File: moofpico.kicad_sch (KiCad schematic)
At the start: 21 parts, among them J1 Conn_01x04, J100 Bus_Apple_II_Card_Side, J2 Micro_SD_Card_Det2, Q1 BS170, SW1 SW_DIP_x02, U2 74F11, U3 74LVC245, U4 74LVC245, U5 74LVC245, U6 RaspberryPi_Pico

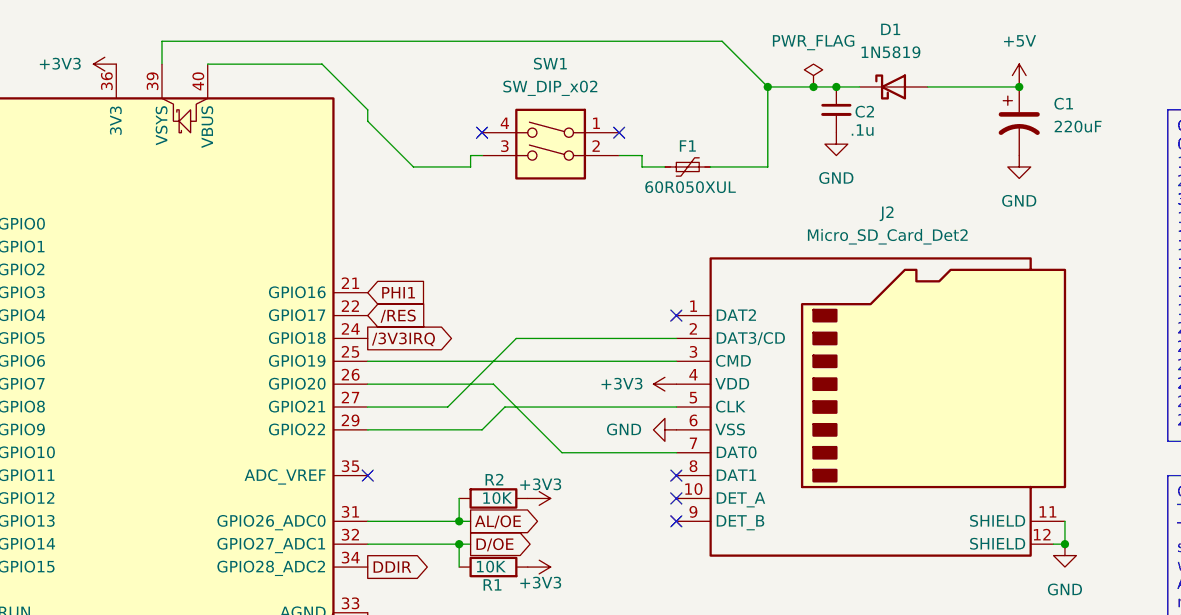
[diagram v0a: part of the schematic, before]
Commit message: checkpoint: kicad 8.0.1, move components around
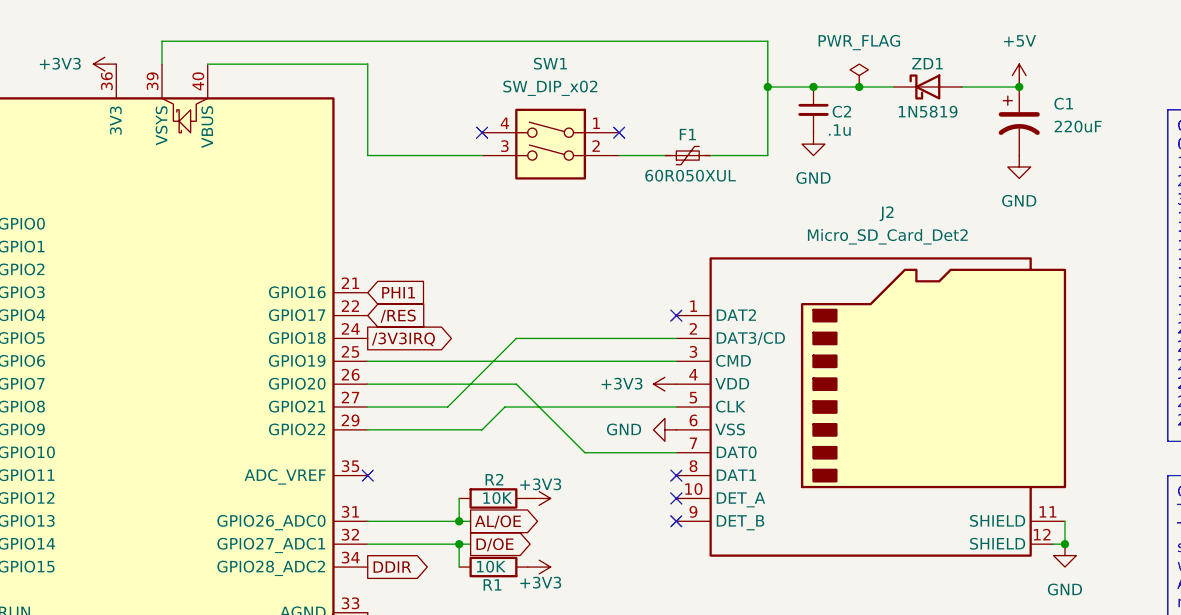
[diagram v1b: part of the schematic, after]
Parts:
- renumbered D1 to ZD1
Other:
- moved on the sheet: C2, F1, ZD1

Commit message: probably voodoo at this point, but: add another decoupling cap (although I seriously doubt it's needed at this point) provide enough space on the board so q1, c1, and f1 can all be bent flat
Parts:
- added C6: .1u, Capacitor_THT:C_Disc_D3.8mm_W2.6mm_P2.50mm, symbol Device:C_Small
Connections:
- net +3V3: now also C6.1
- net GND: now also C6.2
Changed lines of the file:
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@@
 	)
 	(junction
+		(at 41.91 142.24)
+		(diameter 0)
+		(color 0 0 0 0)
+	)
+	(junction
 		(at 57.15 91.44)
 		(diameter 0)
@@
 	(wire
 		(pts
+			(xy 41.91 142.24) (xy 50.8 142.24)
+		)
+		(stroke
+			(width 0)
+			(type default)
+		)
+	)
+	(wire
+		(pts
+			(xy 33.02 137.16) (xy 41.91 137.16)
+		)
+		(stroke
+			(width 0)
+			(type default)
+		)
+	)
+	(wire
+		(pts
 			(xy 118.11 152.4) (xy 119.38 152.4)
 		)
@@
 	(wire
 		(pts
+			(xy 33.02 142.24) (xy 41.91 142.24)
+		)
+		(stroke
+			(width 0)
+			(type default)
+		)
+	)
+	(wire
+		(pts
 			(xy 144.78 177.8) (xy 148.59 177.8)
 		)
@@
 	)
 	(symbol
-		(lib_id "power:GND")
-		(at 50.8 142.24 0)
-		(unit 1)
-		(exclude_from_sim no)
-		(in_bom yes)
-		(on_board yes)
-		(dnp no)
-		(fields_autoplaced yes)
-		(property "Reference" "#PWR038"
-			(at 50.8 148.59 0)
-			(effects
-				(font
-					(size 1.27 1.27)
-				)
-				(hide yes)
-			)
-		)
-		(property "Value" "GND"
-			(at 50.8 147.32 0)
-			(effects
-				(font
-					(size 1.27 1.27)
-				)
-			)
-		)
-		(property "Footprint" ""
-			(at 50.8 142.24 0)
-			(effects
-				(font
-					(size 1.27 1.27)
-				)
-				(hide yes)
-			)
-		)
-		(property "Datasheet" ""
-			(at 50.8 142.24 0)
-			(effects
-				(font
-					(size 1.27 1.27)
-				)
-				(hide yes)
-			)
-		)
-		(property "Description" "Power symbol creates a global label with name \"GND\" , ground"
-			(at 50.8 142.24 0)
-			(effects
-				(font
-					(size 1.27 1.27)
-				)
-				(hide yes)
-			)
-		)
-		(pin "1"
-		)
-		(instances
-			(project "moofpico"
-				(path "/adf04048-7c47-4d7c-943c-c55ccf696419"
-					(reference "#PWR038")
-					(unit 1)
-				)
-			)
-		)
-	)
-	(symbol
 		(lib_id "Transistor_FET:BS170")
 		(at 99.06 172.72 0)
@@
 					(unit 1)
 				)
+			)
+		)
+	)
+	(symbol
+		(lib_id "Device:C_Small")
+		(at 33.02 139.7 0)
+		(unit 1)
+		(exclude_from_sim no)
+		(in_bom yes)
+		(on_board yes)
+		(dnp no)
+		(fields_autoplaced yes)
+		(property "Reference" "C6"
+			(at 35.56 138.4362 0)
+			(effects
+				(font
+					(size 1.27 1.27)
+				)
+				(justify left)
+			)
+		)
+		(property "Value" ".1u"
+			(at 35.56 140.9762 0)
+			(effects
+				(font
+					(size 1.27 1.27)
+				)
+				(justify left)
+			)
+		)
+		(property "Footprint" "Capacitor_THT:C_Disc_D3.8mm_W2.6mm_P2.50mm"
+			(at 33.02 139.7 0)
+			(effects
+				(font
+					(size 1.27 1.27)
+				)
+				(hide yes)
+			)
+		)
+		(property "Datasheet" "https://www.vishay.com/docs/45171/kseries.pdf"
+			(at 33.02 139.7 0)
+			(effects
+				(font
+					(size 1.27 1.27)
+				)
+				(hide yes)
+			)
+		)
+		(property "Description" "K104K10X7RF53L2"
+			(at 33.02 139.7 0)
+			(effects
+				(font
+					(size 1.27 1.27)
+				)
+				(hide yes)
+			)
+		)
+		(pin "1"
+		)
+		(pin "2"
+		)
+		(instances
+			(project "moofpico"
+				(path "/adf04048-7c47-4d7c-943c-c55ccf696419"
+					(reference "C6")
+					(unit 1)
+				)

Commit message: swap nand pin assignments around
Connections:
- net TTLENBL: now also U2.12; no longer U2.8
- net at J100.1 (~{I/O_SELECT}): now also U2.2; no longer U2.9
- net at J100.20 (~{I/O_STROBE}): now also U2.13; no longer U2.11
- net at J100.41 (~{DEVICE_SELECT}): now also U2.1; no longer U2.10
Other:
- moved on the sheet: U2A, U2C
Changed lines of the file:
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@@
 	(wire
 		(pts
-			(xy 161.29 142.24) (xy 176.53 142.24)
-		)
-		(stroke
-			(width 0)
-			(type default)
-		)
-	)
-	(wire
-		(pts
 			(xy 144.78 124.46) (xy 156.21 124.46)
 		)
@@
 	(wire
 		(pts
-			(xy 147.32 142.24) (xy 144.78 142.24)
-		)
-		(stroke
-			(width 0)
-			(type default)
-		)
-	)
-	(wire
-		(pts
 			(xy 199.39 21.59) (xy 203.2 21.59)
 		)
@@
 	(wire
 		(pts
-			(xy 144.78 139.7) (xy 176.53 139.7)
-		)
-		(stroke
-			(width 0)
-			(type default)
-		)
-	)
-	(wire
-		(pts
 			(xy 144.78 29.21) (xy 157.48 29.21)
 		)
@@
 	(wire
 		(pts
-			(xy 144.78 137.16) (xy 156.21 137.16)
-		)
-		(stroke
-			(width 0)
-			(type default)
-		)
-	)
-	(wire
-		(pts
 			(xy 168.91 62.23) (xy 179.07 62.23)
 		)
@@
 	(wire
 		(pts
-			(xy 147.32 144.78) (xy 147.32 142.24)
-		)
-		(stroke
-			(width 0)
-			(type default)
-		)
-	)
-	(wire
-		(pts
 			(xy 144.78 52.07) (xy 179.07 52.07)
 		)
@@
 	(wire
 		(pts
-			(xy 147.32 144.78) (xy 176.53 144.78)
-		)
-		(stroke
-			(width 0)
-			(type default)
-		)
-	)
-	(wire
-		(pts
 			(xy 144.78 69.85) (xy 154.94 69.85)
 		)
@@
 	(wire
 		(pts
-			(xy 156.21 137.16) (xy 161.29 142.24)
-		)
-		(stroke
-			(width 0)
-			(type default)
-		)
-	)
-	(wire
-		(pts
 			(xy 78.74 39.37) (xy 71.12 31.75)
 		)
@@
 	(global_label "TTLENBL"
 		(shape output)
-		(at 191.77 142.24 0)
+		(at 160.02 139.7 0)
 		(fields_autoplaced yes)
 		(effects
@@
 		)
 		(property "Intersheetrefs" "${INTERSHEET_REFS}"
-			(at 202.4961 142.24 0)
+			(at 170.7461 139.7 0)
 			(effects
 				(font
@@
 	(symbol
 		(lib_id "74xx:74LS11")
-		(at 184.15 142.24 0)
+		(at 227.33 140.97 0)
 		(unit 3)
 		(exclude_from_sim no)
@@
 		(fields_autoplaced yes)
 		(property "Reference" "U2"
-			(at 184.1417 133.35 0)
+			(at 227.3217 132.08 0)
 			(effects
 				(font
@@
 		)
 		(property "Value" "74F11"
-			(at 184.1417 135.89 0)
+			(at 227.3217 134.62 0)
 			(effects
 				(font
@@
 		)
 		(property "Footprint" "Package_DIP:DIP-14_W7.62mm_Socket"
-			(at 184.15 142.24 0)
+			(at 227.33 140.97 0)
 			(effects
 				(font
@@
 		)
 		(property "Datasheet" "http://www.ti.com/lit/gpn/sn74LS11"
-			(at 184.15 142.24 0)
+			(at 227.33 140.97 0)
 			(effects
 				(font
@@
 		)
 		(property "Description" "Triple 3-input AND"
-			(at 184.15 142.24 0)
+			(at 227.33 140.97 0)
 			(effects
 				(font
@@
 	(symbol
 		(lib_id "74xx:74LS11")
-		(at 227.33 140.97 0)
+		(at 152.4 139.7 0)
 		(unit 1)
 		(exclude_from_sim no)
@@
 		(on_board yes)
 		(dnp no)
-		(fields_autoplaced yes)
 		(property "Reference" "U2"
-			(at 227.3217 132.08 0)
+			(at 151.892 139.7 0)
 			(effects
 				(font
@@
 		)
 		(property "Value" "74F11"
-			(at 227.3217 134.62 0)
+			(at 152.4 144.526 0)
 			(effects
 				(font
@@
 		)
 		(property "Footprint" "Package_DIP:DIP-14_W7.62mm_Socket"
-			(at 227.33 140.97 0)
+			(at 152.4 139.7 0)
 			(effects
 				(font
@@
 		)
 		(property "Datasheet" "http://www.ti.com/lit/gpn/sn74LS11"
-			(at 227.33 140.97 0)
+			(at 152.4 139.7 0)
 			(effects
 				(font
@@
 		)
 		(property "Description" "Triple 3-input AND"
-			(at 227.33 140.97 0)
+			(at 152.4 139.7 0)
 			(effects
 				(font

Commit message: ground unused NAND inputs
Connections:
- net GND: now also U2.10, U2.11, U2.3, U2.4, U2.5, U2.9
- no-connect marks 34 -> 28
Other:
- note added: "Internally pulled high"
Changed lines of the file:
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@@
 	)
 	(junction
+		(at 219.71 153.67)
+		(diameter 0)
+		(color 0 0 0 0)
+	)
+	(junction
 		(at 154.94 72.39)
 		(diameter 0)
@@
 	)
 	(junction
+		(at 219.71 158.75)
+		(diameter 0)
+		(color 0 0 0 0)
+	)
+	(junction
 		(at 209.55 124.46)
 		(diameter 0)
@@
 	)
 	(junction
+		(at 101.6 181.61)
+		(diameter 0)
+		(color 0 0 0 0)
+	)
+	(junction
+		(at 219.71 140.97)
+		(diameter 0)
+		(color 0 0 0 0)
+	)
+	(junction
 		(at 189.23 21.59)
 		(diameter 0)
@@
 	)
 	(junction
+		(at 219.71 156.21)
+		(diameter 0)
+		(color 0 0 0 0)
+	)
+	(junction
 		(at 209.55 99.06)
 		(diameter 0)
@@
 		(color 0 0 0 0)
 	)
+	(junction
+		(at 219.71 143.51)
+		(diameter 0)
+		(color 0 0 0 0)
+	)
 	(no_connect
 		(at 119.38 172.72)
@@
 	)
 	(no_connect
-		(at 219.71 140.97)
-	)
-	(no_connect
-		(at 219.71 153.67)
-	)
-	(no_connect
 		(at 119.38 144.78)
 	)
@@
 	)
 	(no_connect
-		(at 219.71 143.51)
-	)
-	(no_connect
 		(at 172.72 26.67)
 	)
@@
 	)
 	(no_connect
-		(at 99.06 80.01)
-	)
-	(no_connect
 		(at 179.07 64.77)
 	)
 	(no_connect
-		(at 219.71 158.75)
-	)
-	(no_connect
 		(at 144.78 64.77)
 	)
@@
 	)
 	(no_connect
+		(at 99.06 80.01)
+	)
+	(no_connect
 		(at 134.62 190.5)
 	)
@@
 	)
 	(no_connect
-		(at 219.71 138.43)
-	)
-	(no_connect
 		(at 119.38 177.8)
 	)
-	(no_connect
-		(at 219.71 156.21)
-	)
 	(wire
 		(pts
@@
 	(wire
 		(pts
+			(xy 219.71 138.43) (xy 219.71 140.97)
+		)
+		(stroke
+			(width 0)
+			(type default)
+		)
+	)
+	(wire
+		(pts
 			(xy 189.23 21.59) (xy 194.31 21.59)
 		)
@@
 	(wire
 		(pts
+			(xy 219.71 140.97) (xy 219.71 143.51)
+		)
+		(stroke
+			(width 0)
+			(type default)
+		)
+	)
+	(wire
+		(pts
 			(xy 154.94 69.85) (xy 156.21 69.85)
 		)
@@
 	(wire
 		(pts
+			(xy 219.71 156.21) (xy 219.71 158.75)
+		)
+		(stroke
+			(width 0)
+			(type default)
+		)
+	)
+	(wire
+		(pts
 			(xy 160.02 57.15) (xy 157.48 59.69)
 		)
@@
 	(wire
 		(pts
-			(xy 101.6 182.88) (xy 101.6 177.8)
+			(xy 101.6 182.88) (xy 101.6 181.61)
 		)
 		(stroke
@@
 	(wire
 		(pts
+			(xy 219.71 153.67) (xy 219.71 156.21)
+		)
+		(stroke
+			(width 0)
+			(type default)
+		)
+	)
+	(wire
+		(pts
 			(xy 118.11 165.1) (xy 119.38 165.1)
 		)
@@
 	(wire
 		(pts
+			(xy 93.98 181.61) (xy 101.6 181.61)
+		)
+		(stroke
+			(width 0)
+			(type default)
+		)
+	)
+	(wire
+		(pts
 			(xy 161.29 54.61) (xy 168.91 62.23)
 		)
@@
 	(wire
 		(pts
+			(xy 219.71 143.51) (xy 219.71 153.67)
+		)
+		(stroke
+			(width 0)
+			(type default)
+		)
+	)
+	(wire
+		(pts
 			(xy 160.02 57.15) (xy 179.07 57.15)
 		)
@@
 	(wire
 		(pts
+			(xy 101.6 181.61) (xy 101.6 177.8)
+		)
+		(stroke
+			(width 0)
+			(type default)
+		)
+	)
+	(wire
+		(pts
+			(xy 219.71 158.75) (xy 219.71 163.83)
+		)
+		(stroke
+			(width 0)
+			(type default)
+		)
+	)
+	(wire
+		(pts
 			(xy 144.78 69.85) (xy 154.94 69.85)
 		)
@@
 		)
 	)
+	(text "Internally pulled high"
+		(exclude_from_sim no)
+		(at 88.392 81.28 0)
+		(effects
+			(font
+				(size 1.27 1.27)
+			)
+		)
+	)
 	(global_label "AD3"
 		(shape tri_state)
@@
 	)
 	(symbol
-		(lib_id "power:GND")
-		(at 93.98 181.61 0)
-		(unit 1)
-		(exclude_from_sim no)
-		(in_bom yes)
-		(on_board yes)
-		(dnp no)
-		(fields_autoplaced yes)
-		(property "Reference" "#PWR032"
-			(at 93.98 187.96 0)
-			(effects
-				(font
-					(size 1.27 1.27)
-				)
-				(hide yes)
-			)
-		)
-		(property "Value" "GND"
-			(at 93.9801 185.42 90)
-			(effects
-				(font
-					(size 1.27 1.27)
-				)
-				(justify right)
-			)
-		)
-		(property "Footprint" ""
-			(at 93.98 181.61 0)
-			(effects
-				(font
-					(size 1.27 1.27)
-				)
-				(hide yes)
-			)
-		)
-		(property "Datasheet" ""
-			(at 93.98 181.61 0)
-			(effects
-				(font
-					(size 1.27 1.27)
-				)
-				(hide yes)
-			)
-		)
-		(property "Description" "Power symbol creates a global label with name \"GND\" , ground"
-			(at 93.98 181.61 0)
-			(effects
-				(font
-					(size 1.27 1.27)
-				)
-				(hide yes)
-			)
-		)
-		(pin "1"
-		)
-		(instances
-			(project "moofpico"
-				(path "/adf04048-7c47-4d7c-943c-c55ccf696419"
-					(reference "#PWR032")
-					(unit 1)
-				)
-			)
-		)
-	)
-	(symbol
 		(lib_id "74xx:74LS11")
 		(at 152.4 139.7 0)
@@
 					(unit 1)
 				)
+			)
+		)
+	)
+	(symbol
+		(lib_id "power:GND")
+		(at 219.71 163.83 0)
+		(unit 1)
+		(exclude_from_sim no)
+		(in_bom yes)
+		(on_board yes)
+		(dnp no)
+		(fields_autoplaced yes)
+		(property "Reference" "#PWR04"
+			(at 219.71 170.18 0)
+			(effects
+				(font
+					(size 1.27 1.27)
+				)
+				(hide yes)
+			)
+		)
+		(property "Value" "GND"
+			(at 219.71 168.91 0)
+			(effects
+				(font
+					(size 1.27 1.27)
+				)
+			)
+		)
+		(property "Footprint" ""
+			(at 219.71 163.83 0)
+			(effects
+				(font
+					(size 1.27 1.27)
+				)
+				(hide yes)
+			)
+		)
+		(property "Datasheet" ""
+			(at 219.71 163.83 0)
+			(effects
+				(font
+					(size 1.27 1.27)
+				)
+				(hide yes)
+			)
+		)
+		(property "Description" "Power symbol creates a global label with name \"GND\" , ground"
+			(at 219.71 163.83 0)
+			(effects
+				(font
+					(size 1.27 1.27)
+				)
+				(hide yes)
+			)
+		)
+		(pin "1"
+		)
+		(instances
+			(project "moofpico"
+				(path "/adf04048-7c47-4d7c-943c-c55ccf696419"
+					(reference "#PWR04")
+					(unit 1)
+				)
